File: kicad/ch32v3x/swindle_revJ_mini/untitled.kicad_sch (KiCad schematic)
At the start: 7 parts, among them J10 Debug port, J3 Dbg, J5 Debug port, J6 Debug port, J7 Conn_01x03_Pin, J8 Debug port, J9 Conn_01x03_Pin

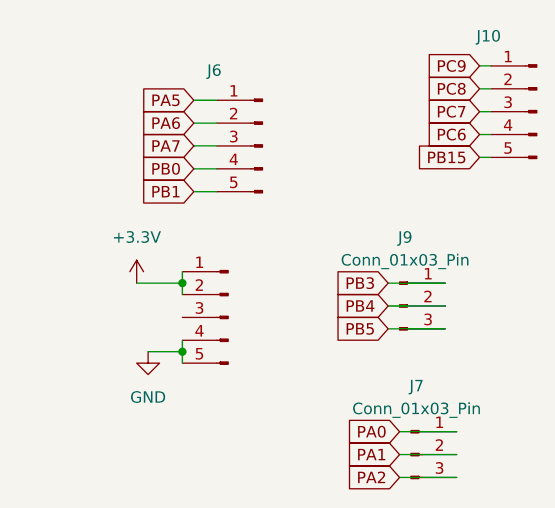
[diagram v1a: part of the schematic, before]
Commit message: Kicad update: ch32: update pcb , add boot pin control ch32: Ground PB2 so that the internal bootloader is on USB rp_zero_mini :add mostfet to rp zero mini
general update
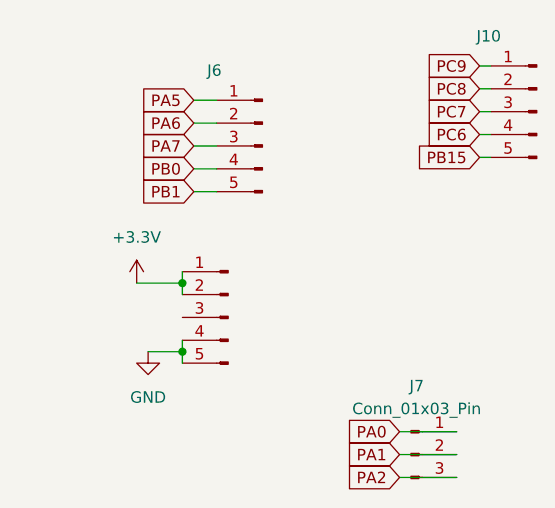
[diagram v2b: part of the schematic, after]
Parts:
- removed J9: Conn_01x03_Pin, Connector_PinSocket_1.27mm:PinSocket_1x03_P1.27mm_Vertical, symbol Connector:Conn_01x03_Pin
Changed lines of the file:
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@@
-	(wire
-		(pts
-			(xy 107.95 87.63) (xy 114.3 87.63)
-		)
-		(stroke
-			(width 0)
-			(type default)
-		)
-	)
 	(wire
 		(pts
@@
 	(wire
 		(pts
-			(xy 107.95 90.17) (xy 114.3 90.17)
-		)
-		(stroke
-			(width 0)
-			(type default)
-		)
-	)
-	(wire
-		(pts
 			(xy 118.11 66.04) (xy 119.38 66.04)
 		)
@@
 	(wire
 		(pts
-			(xy 107.95 85.09) (xy 114.3 85.09)
-		)
-		(stroke
-			(width 0)
-			(type default)
-		)
-	)
-	(wire
-		(pts
 			(xy 118.11 68.58) (xy 119.38 68.58)
 		)
@@
 		)
 	)
-	(global_label "PB3"
-		(shape input)
-		(at 107.95 85.09 180)
-		(fields_autoplaced yes)
-		(effects
-			(font
-				(size 1.27 1.27)
-			)
-			(justify right)
-		)
-		(property "Intersheetrefs" "${INTERSHEET_REFS}"
-			(at 101.2153 85.09 0)
-			(hide yes)
-			(show_name no)
-			(do_not_autoplace no)
-			(effects
-				(font
-					(size 1.27 1.27)
-				)
-				(justify right)
-			)
-		)
-	)
-	(global_label "PB5"
-		(shape input)
-		(at 107.95 90.17 180)
-		(fields_autoplaced yes)
-		(effects
-			(font
-				(size 1.27 1.27)
-			)
-			(justify right)
-		)
-		(property "Intersheetrefs" "${INTERSHEET_REFS}"
-			(at 101.2153 90.17 0)
-			(hide yes)
-			(show_name no)
-			(do_not_autoplace no)
-			(effects
-				(font
-					(size 1.27 1.27)
-				)
-				(justify right)
-			)
-		)
-	)
 	(global_label "OUT_SWDCLK"
 		(shape input)
@@
 		(property "Intersheetrefs" "${INTERSHEET_REFS}"
 			(at 79.6253 72.39 0)
-			(hide yes)
-			(show_name no)
-			(do_not_autoplace no)
-			(effects
-				(font
-					(size 1.27 1.27)
-				)
-				(justify right)
-			)
-		)
-	)
-	(global_label "PB4"
-		(shape input)
-		(at 107.95 87.63 180)
-		(fields_autoplaced yes)
-		(effects
-			(font
-				(size 1.27 1.27)
-			)
-			(justify right)
-		)
-		(property "Intersheetrefs" "${INTERSHEET_REFS}"
-			(at 101.2153 87.63 0)
 			(hide yes)
 			(show_name no)
@@
 					(unit 1)
 				)
-			)
-		)
-	)
-	(symbol
-		(lib_id "Connector:Conn_01x03_Pin")
-		(at 109.22 87.63 0)
-		(unit 1)
-		(body_style 1)
-		(exclude_from_sim no)
-		(in_bom yes)
-		(on_board yes)
-		(in_pos_files yes)
-		(dnp no)
-		(fields_autoplaced yes)
-		(property "Reference" "J9"
-			(at 109.855 80.01 0)
-			(show_name no)
-			(do_not_autoplace no)
-			(effects
-				(font
-					(size 1.27 1.27)
-				)
-			)
-		)
-		(property "Value" "Conn_01x03_Pin"
-			(at 109.855 82.55 0)
-			(show_name no)
-			(do_not_autoplace no)
-			(effects
-				(font
-					(size 1.27 1.27)
-				)
-			)
-		)
-		(property "Footprint" "Connector_PinSocket_1.27mm:PinSocket_1x03_P1.27mm_Vertical"
-			(at 109.22 87.63 0)
-			(hide yes)
-			(show_name no)
-			(do_not_autoplace no)
-			(effects
-				(font
-					(size 1.27 1.27)
-				)
-			)
-		)
-		(property "Datasheet" ""
-			(at 109.22 87.63 0)
-			(hide yes)
-			(show_name no)
-			(do_not_autoplace no)
-			(effects
-				(font
-					(size 1.27 1.27)
-				)
-			)
-		)
-		(property "Description" "Generic connector, single row, 01x03, script generated"
-			(at 109.22 87.63 0)
-			(hide yes)
-			(show_name no)
-			(do_not_autoplace no)
-			(effects
-				(font
-					(size 1.27 1.27)
-				)
-			)
-		)
-		(pin "3"
-		)
-		(pin "2"
-		)
-		(pin "1"
-		)
-		(instances
-			(project "swindle_ch32_revJ_mini"
-				(path "/fbe443d6-6d74-4abc-9dee-16e0160553bc/ed84c662-1e11-4141-9b01-0918066453ad"
-					(reference "J9")
-					(unit 1)
-				)
